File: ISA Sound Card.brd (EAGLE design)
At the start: 163.2 x 108.6 mm, 89 parts, among them IC1 74LS07D, IC10 4051D, IC11 4051D, IC2 74AHC1G07DBV, IC3 74AC14D, IC4 74LVC1G125DBV, IC6 MCP3004, IC8 4051D, IC9 4051D, U1 PCM1808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

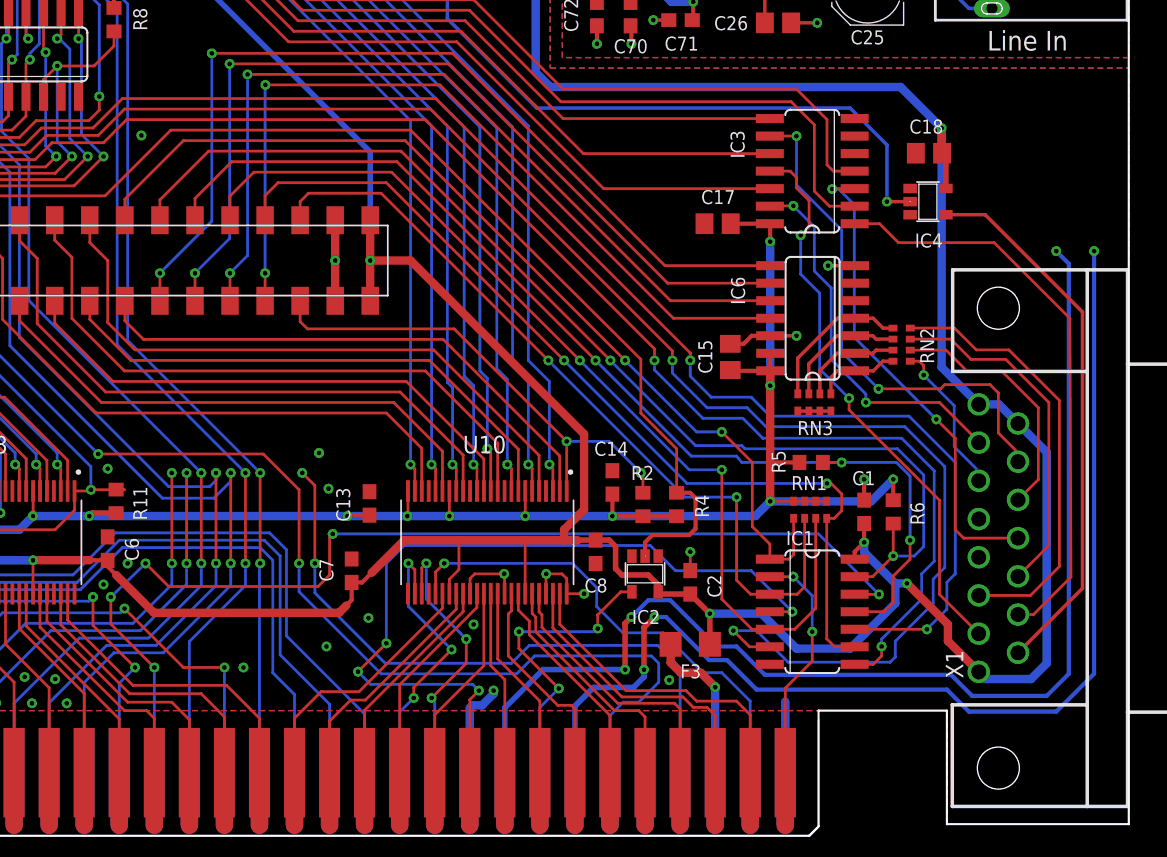
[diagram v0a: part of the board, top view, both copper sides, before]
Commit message: Added missing pullups to the Joystick button inputs
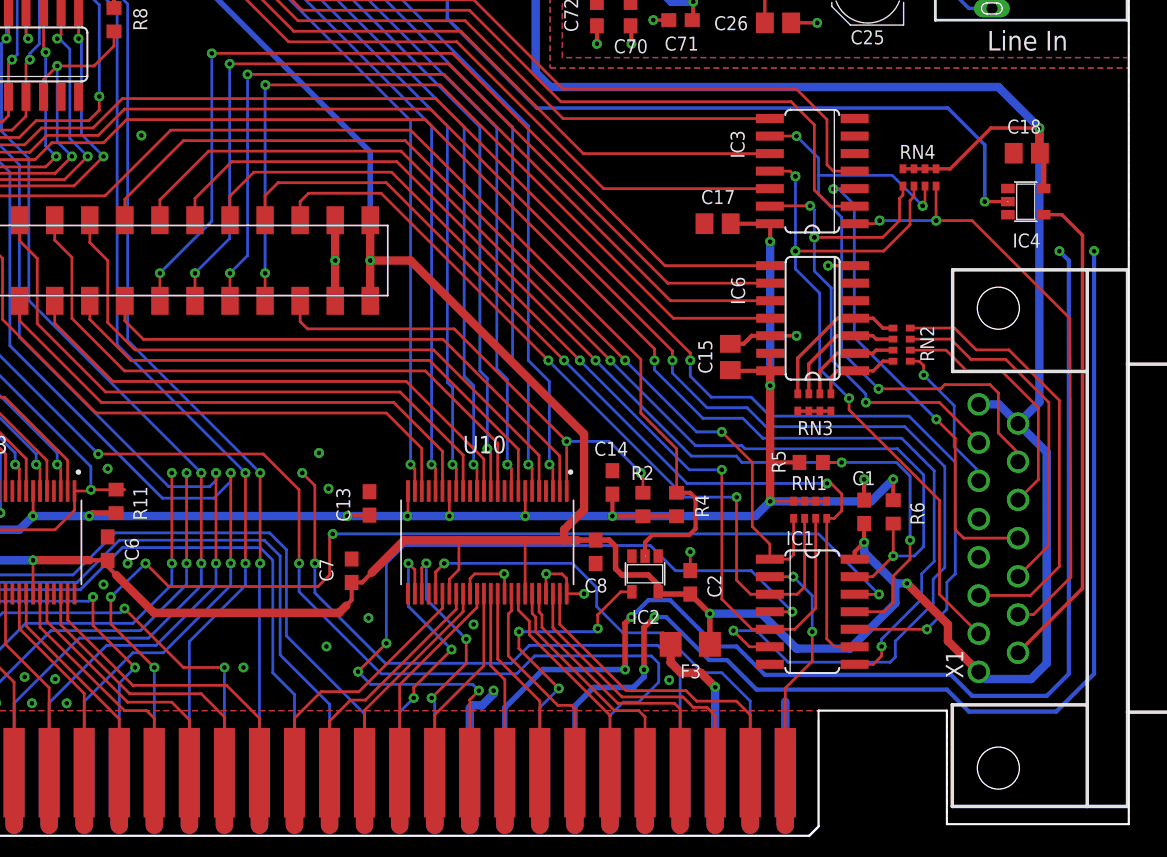
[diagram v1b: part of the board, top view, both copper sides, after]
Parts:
- added RN4: 10K, resistor-dil:0603-ARC
- moved C18 7.09 mm to (176.4, 57.8)
- moved IC4 7.09 mm to (176.3, 54.3)
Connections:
- net +5V: now also RN4.5, RN4.6, RN4.7, RN4.8
- net JOY_B1_N: now also RN4.1
- net JOY_B2_N: now also RN4.2
- net JOY_B3_N: now also RN4.3
- net JOY_B4_N: now also RN4.4
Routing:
- net +5V: track 609.1 -> 628.2 mm
- net JOY_B2_N: track 41.2 -> 52.7 mm, vias 2 -> 3
- net JOY_B1_N: track 27.6 -> 37.6 mm, vias 2 -> 3
- net JOY_B3_N: track 37.3 -> 47.3 mm, vias 2 -> 3
- net FPGA_MIDI_TXD: track 99.2 -> 106.3 mm
- net MIDI_TXD: track 39.4 -> 35.6 mm
- net JOY_B4_N: track 42.1 -> 44.8 mm, vias 0 -> 2
- net IRQ7: track 89.3 -> 88.5 mm
